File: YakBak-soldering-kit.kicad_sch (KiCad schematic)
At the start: 4 parts, among them SW1 SW_Push, U1 MOUDLE-SEEEDUINO-XIAO-ESP32C3, U2 Adafruit 2130 - PAM8302, U3 Electret Microphone Amp Module

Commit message: Finished the schematic. Review time!
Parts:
- added C1: 100 nF, symbol Device:C_Small
- added H1, H2, H3, H4: MountingHole, symbol Mechanical:MountingHole
- added J1, J2: Conn_01x07_Socket, symbol Connector:Conn_01x07_Socket
- added R1: 100 ohms, symbol Device:R_Small_US
- added SW2: Play, symbol Switch:SW_Push
- SW1: value SW_Push -> Say
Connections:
- net +3.3V: now also U1.12 (3V3), U3. (VCC), J1.5 (Pin_5)
- net GND: now also SW1.1, U1.13 (GND), U2.1 (GND), U2.4 (A-), U3. (VCC), C1.2, J1.6 (Pin_6), SW2.1
- net D8: now reaches SW1.2
- net D8: now also U1.9 (PA7_A8_D8_SCK), J1.2 (Pin_2)
- net D0: now reaches U1.1 (PA02_A0_D0)
- net D0: now also U3. (VCC), J2.1 (Pin_1)
- net D9: now reaches U1.10 (PA5_A9_D9_MISO)
- net D9: now also U2.3 (Shutdown), J1.3 (Pin_3)
- net D10: now reaches U1.11 (PA6_A10_D10_MOSI)
- net D10: now also J1.4 (Pin_4), R1.1
- net +5V: now reaches U1.14 (5V)
- net +5V: now also U2.2 (Vin), J1.7 (Pin_7)
- net D1: now reaches U1.2 (PA4_A1_D1)
- net D1: now also J2.2 (Pin_2)
- net D2: now reaches U1.3 (PA10_A2_D2)
- net D2: now also J2.3 (Pin_3)
- net D3: now reaches U1.4 (PA11_A3_D3)
- net D3: now also J2.4 (Pin_4)
- net D4: now reaches U1.5 (PA8_A4_D4_SDA)
- net D4: now also J2.5 (Pin_5)
- net D5: now reaches U1.6 (PA9_A5_D5_SCL)
- net D5: now also J2.6 (Pin_6)
- net D6: now reaches U1.7 (PB08_A6_D6_TX)
- net D6: now also J2.7 (Pin_7)
- net D7: now reaches U1.8 (PB09_A7_D7_RX)
- net D7: now also J1.1 (Pin_1), SW2.2
- net at U2.5 (A+): now also C1.1, R1.2
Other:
- note added: "Easy hacking through-holes :)"
- note added: "Pull shutdown low to disable amp"
- note added: "We can hide the designators on the board"
- moved on the sheet: SW1, U2, U3

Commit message: changes to schematic to fix ERC check and addition of PCB edges.
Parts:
- removed U1: MOUDLE-SEEEDUINO-XIAO-ESP32C3, MOUDLE14P-SMD-2.54-21X17.8MM, symbol MOUDLE-SEEEDUINO-XIAO-ESP32C3:MOUDLE-SEEEDUINO-XIAO-ESP32C3
- removed U2: Adafruit 2130 - PAM8302, symbol my_library:Adafruit_2130_PAM8302A_2.5W_Class_D_Amplifier_Module
- removed U3: Electret Microphone Amp Module, symbol my_library:Electret_Mic_Module
- added U1: MOUDLE-SEEEDUINO-XIAO-ESP32C3, XIAO_ESP32C3_PCB:MOUDLE14P-SMD-2.54-21X17.8MM, symbol YakBak-soldering-kit-eagle-import:MODULE-SEEEDUINO-XIAO-ESP32C3_all_passive
- added U2: Electret Microphone Amp Module, Connector_PinSocket_2.54mm:PinSocket_1x03_P2.54mm_Vertical, symbol YakBak-soldering-kit-eagle-import:Electret_Mic_Module_all_pins_passive
- added U3: Adafruit 2130 - PAM8302, Connector_PinSocket_2.54mm:PinSocket_1x05_P2.54mm_Vertical, symbol YakBak-soldering-kit-eagle-import:Adafruit_2130_PAM8302A_2.5W_Class_D_Amplifier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
- C1: footprint (none) -> Capacitor_THT:CP_Radial_D12.5mm_P5.00mm
- H1, H2, H3, H4: footprint (none) -> MountingHole:MountingHole_2.5mm
- J1, J2: footprint (none) -> Connector_PinSocket_2.54mm:PinSocket_1x07_P2.54mm_Vertical
- R1: footprint (none) -> Resistor_THT:R_Axial_DIN0411_L9.9mm_D3.6mm_P15.24mm_Horizontal
- SW1, SW2: footprint (none) -> Button_Switch_THT:SW_PUSH_6mm
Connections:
- net +3.3V: now also U1.12 (3V3), U2. (VCC)
- net +5V: now also U1.14 (5V), U3.2 (Vin)
- net D0: now also U1.1 (PA02_A0_D0), U2. (VCC)
- net D1: now also U1.2 (PA4_A1_D1)
- net D10: now also U1.11 (PA6_A10_D10_MOSI)
- net D2: now also U1.3 (PA10_A2_D2)
- net D3: now also U1.4 (PA11_A3_D3)
- net D4: now also U1.5 (PA8_A4_D4_SDA)
- net D5: now also U1.6 (PA9_A5_D5_SCL)
- net D6: now also U1.7 (PB08_A6_D6_TX)
- net D7: now also U1.8 (PB09_A7_D7_RX)
- net D8: now also U1.9 (PA7_A8_D8_SCK)
- net D9: now also U1.10 (PA5_A9_D9_MISO), U3.3 (Shutdown)
- net GND: now also U1.13 (GND), U2. (VCC), U3.1 (GND), U3.4 (A-)
- net at C1.1, R1.2: now also U3.5 (A+)

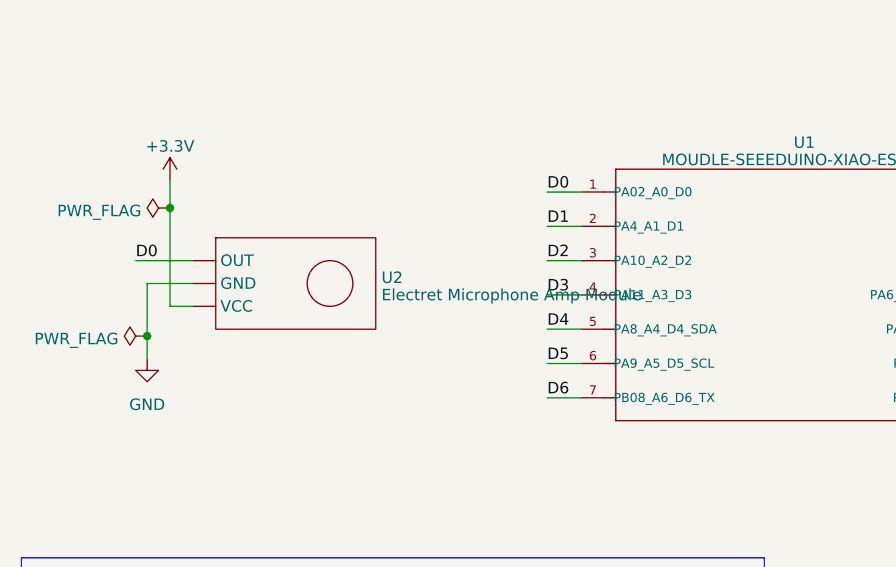
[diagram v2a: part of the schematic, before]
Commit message: finished draft layout and updated missing symbols/footprints
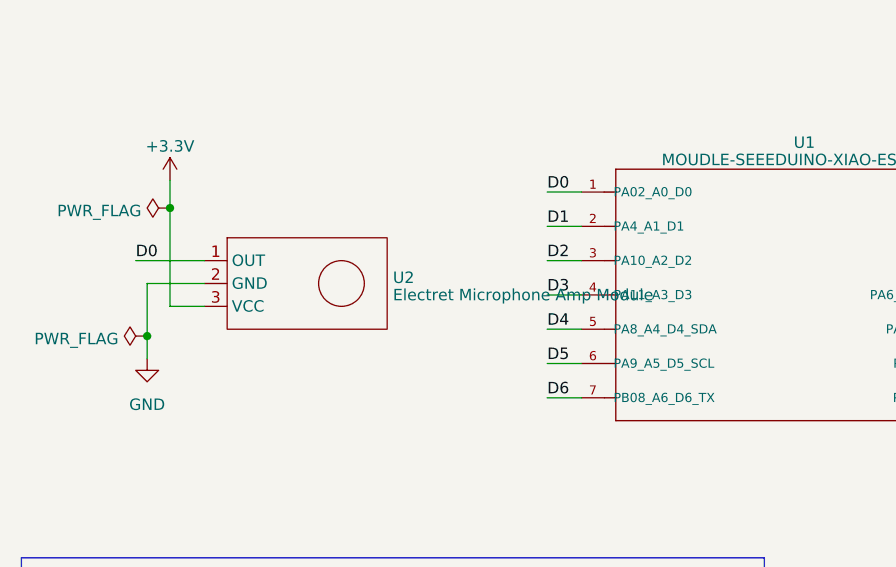
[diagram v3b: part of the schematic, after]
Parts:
- C1: footprint Capacitor_THT:CP_Radial_D12.5mm_P5.00mm -> Capacitor_THT:C_Disc_D5.1mm_W3.2mm_P5.00mm
- R1: footprint Resistor_THT:R_Axial_DIN0411_L9.9mm_D3.6mm_P15.24mm_Horizontal -> Resistor_THT:R_Axial_DIN0204_L3.6mm_D1.6mm_P7.62mm_Horizontal
- U1: footprint XIAO_ESP32C3_PCB:MOUDLE14P-SMD-2.54-21X17.8MM -> xiao ESP32C3_PCB:MOUDLE14P-SMD-2.54-21X17.8MM
- U3: footprint Connector_PinSocket_2.54mm:PinSocket_1x05_P2.54mm_Vertical -> Connector_PinHeader_2.54mm:PinHeader_1x05_P2.54mm_Vertical
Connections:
- net +3.3V: now also U2.3 (VCC); no longer U2. (VCC)
- net D0: now also U2.1 (OUT); no longer U2. (VCC)
- net GND: now also U2.2 (GND); no longer U2. (VCC)
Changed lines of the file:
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@@
   (junction (at 147.32 60.96) (diameter 0) (color 0 0 0 0)
   )
-  (wire (pts (xy 21.59 57.15) (xy 27.94 57.15))
-    (stroke (width 0) (type default))
-  )
   (wire (pts (xy 120.65 60.96) (xy 137.16 60.96))
     (stroke (width 0) (type default))
@@
     (stroke (width 0) (type default))
   )
-  (wire (pts (xy 22.86 59.69) (xy 27.94 59.69))
-    (stroke (width 0) (type default))
-  )
   (wire (pts (xy 162.56 66.04) (xy 170.18 66.04))
     (stroke (width 0) (type default))
@@
     (stroke (width 0) (type default))
   )
-  (wire (pts (xy 25.4 62.23) (xy 27.94 62.23))
-    (stroke (width 0) (type default))
-  )
   (wire (pts (xy 24.13 104.14) (xy 24.13 106.68))
     (stroke (width 0) (type default))
@@
     (stroke (width 0) (type default))
   )
+  (wire (pts (xy 22.86 59.69) (xy 29.21 59.69))
+    (stroke (width 0) (type default))
+  )
   (wire (pts (xy 147.32 60.96) (xy 147.32 62.23))
     (stroke (width 0) (type default))
@@
     (stroke (width 0) (type default))
   )
+  (wire (pts (xy 21.59 57.15) (xy 29.21 57.15))
+    (stroke (width 0) (type default))
+  )
   (wire (pts (xy 25.4 119.38) (xy 27.94 119.38))
     (stroke (width 0) (type default))
@@
     (stroke (width 0) (type default))
   )
+  (wire (pts (xy 25.4 62.23) (xy 29.21 62.23))
+    (stroke (width 0) (type default))
+  )
   (wire (pts (xy 25.4 51.308) (xy 25.4 62.23))
     (stroke (width 0) (type default))
@@
       (effects (font (size 1.27 1.27)))
     )
-    (property "Footprint" "XIAO_ESP32C3_PCB:MOUDLE14P-SMD-2.54-21X17.8MM" (at 96.52 60.96 0)
+    (property "Footprint" "xiao ESP32C3_PCB:MOUDLE14P-SMD-2.54-21X17.8MM" (at 96.52 60.96 0)
       (effects (font (size 1.27 1.27)) (justify bottom) hide)
     )
@@
     )
   )
-  (symbol (lib_id "YakBak-soldering-kit-eagle-import:Electret_Mic_Module_all_pins_passive") (at 39.37 59.69 0) (unit 1)
-    (in_bom yes) (on_board yes) (dnp no) (fields_autoplaced)
-    (property "Reference" "U2" (at 48.895 59.0463 0)
-      (effects (font (size 1.27 1.27)) (justify left))
-    )
-    (property "Value" "Electret Microphone Amp Module" (at 48.895 60.9673 0)
-      (effects (font (size 1.27 1.27)) (justify left))
-    )
-    (property "Footprint" "Connector_PinSocket_2.54mm:PinSocket_1x03_P2.54mm_Vertical" (at 27.94 69.85 0)
-      (effects (font (size 1.27 1.27)) hide)
-    )
-    (property "Datasheet" "" (at 27.94 62.23 0)
-      (effects (font (size 1.27 1.27)) hide)
-    )
-    (pin "")
-    (pin "")
-    (pin "")
+  (symbol (lib_id "YakBak-soldering-kit-eagle-import:Electret_Mic_Module_all_pins_passive") (at 40.64 59.69 0) (unit 1)
+    (in_bom yes) (on_board yes) (dnp no) (fields_autoplaced)
+    (property "Reference" "U2" (at 50.165 59.0463 0)
+      (effects (font (size 1.27 1.27)) (justify left))
+    )
+    (property "Value" "Electret Microphone Amp Module" (at 50.165 60.9673 0)
+      (effects (font (size 1.27 1.27)) (justify left))
+    )
+    (property "Footprint" "Connector_PinSocket_2.54mm:PinSocket_1x03_P2.54mm_Vertical" (at 29.21 69.85 0)
+      (effects (font (size 1.27 1.27)) hide)
+    )
+    (property "Datasheet" "" (at 29.21 62.23 0)
+      (effects (font (size 1.27 1.27)) hide)
+    )
+    (pin "1")
+    (pin "2")
+    (pin "3")
     (instances
       (project "YakBak-soldering-kit"
@@
       (effects (font (size 1.27 1.27)) (justify left))
     )
-    (property "Footprint" "Connector_PinSocket_2.54mm:PinSocket_1x05_P2.54mm_Vertical" (at 177.8 81.28 0)
+    (property "Footprint" "Connector_PinHeader_2.54mm:PinHeader_1x05_P2.54mm_Vertical" (at 177.8 81.28 0)
       (effects (font (size 1.27 1.27)) hide)
     )
@@
       (effects (font (size 1.27 1.27)))
     )
-    (property "Footprint" "Resistor_THT:R_Axial_DIN0411_L9.9mm_D3.6mm_P15.24mm_Horizontal" (at 139.7 60.96 0)
+    (property "Footprint" "Resistor_THT:R_Axial_DIN0204_L3.6mm_D1.6mm_P7.62mm_Horizontal" (at 139.7 60.96 0)
       (effects (font (size 1.27 1.27)) hide)
     )
@@
       (effects (font (size 1.27 1.27)) (justify left))
     )
-    (property "Footprint" "Capacitor_THT:CP_Radial_D12.5mm_P5.00mm" (at 147.32 64.77 0)
-      (effects (font (size 1.27 1.27)) hide)
-    )
+    (property "Footprint" "Capacitor_THT:C_Disc_D5.1mm_W3.2mm_P5.00mm" (at 147.32 64.77 0)
+      (effects (font (size 1.27 1.27)) hide)
+    )
